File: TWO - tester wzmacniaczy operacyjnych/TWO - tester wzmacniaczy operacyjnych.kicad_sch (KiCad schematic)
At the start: 0 parts

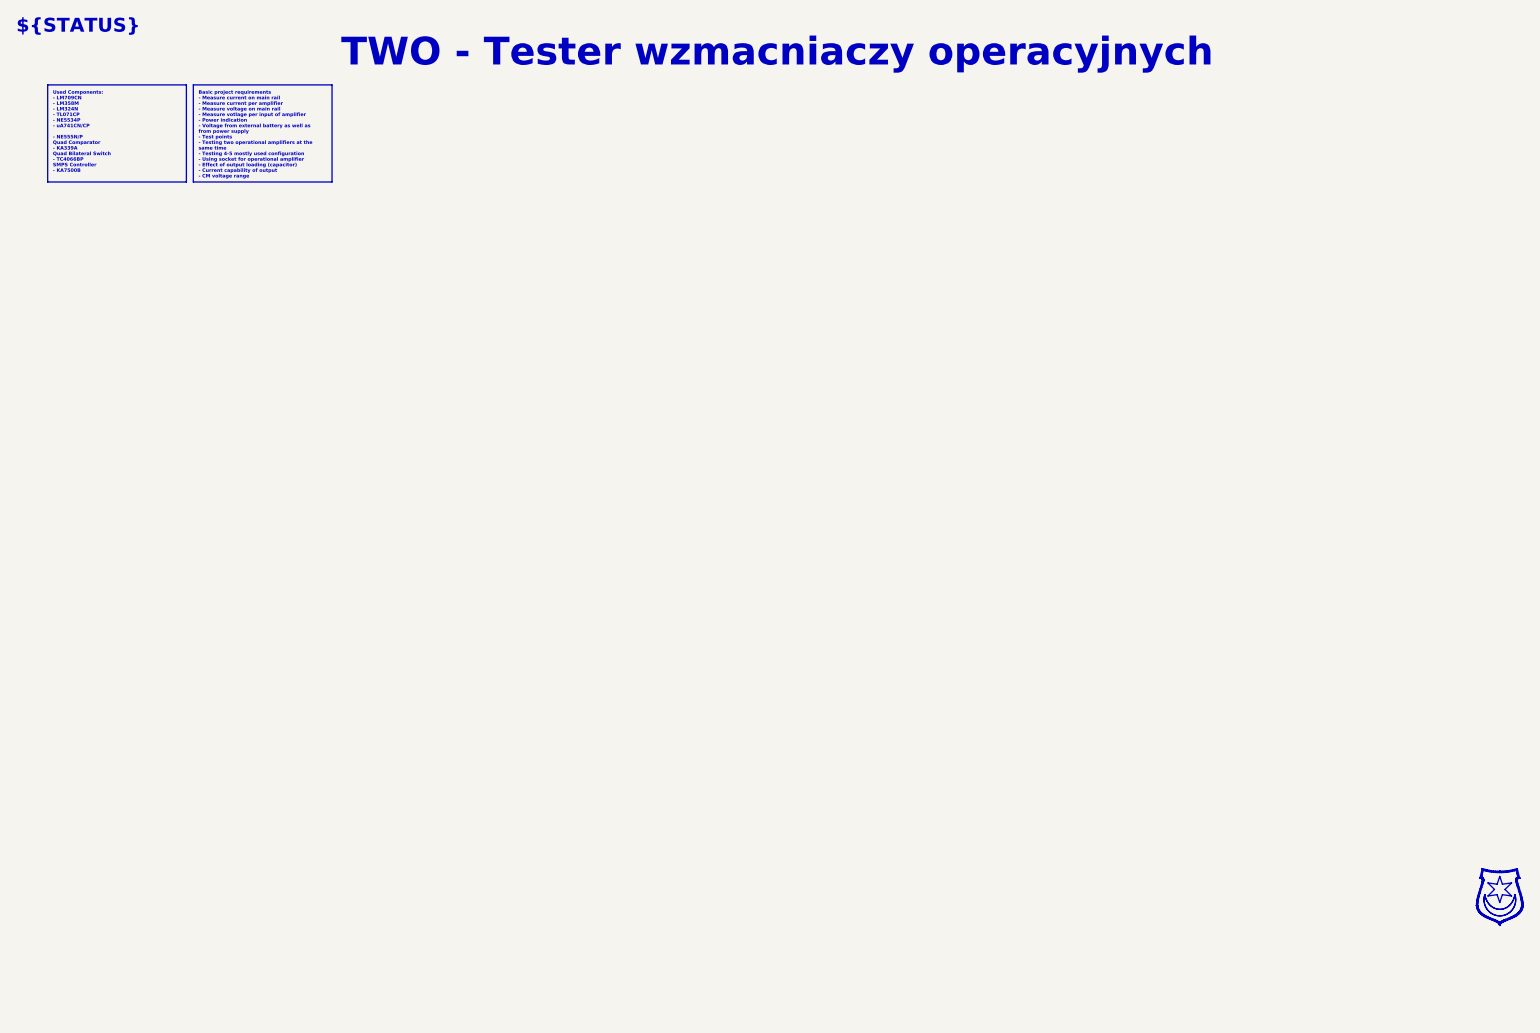
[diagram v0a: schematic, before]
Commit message: Added 0R resistor for 0V potential to measure current, Added on a schematic LM358M, LM324N, TL071CP, NE5534P, uA741CN/CP
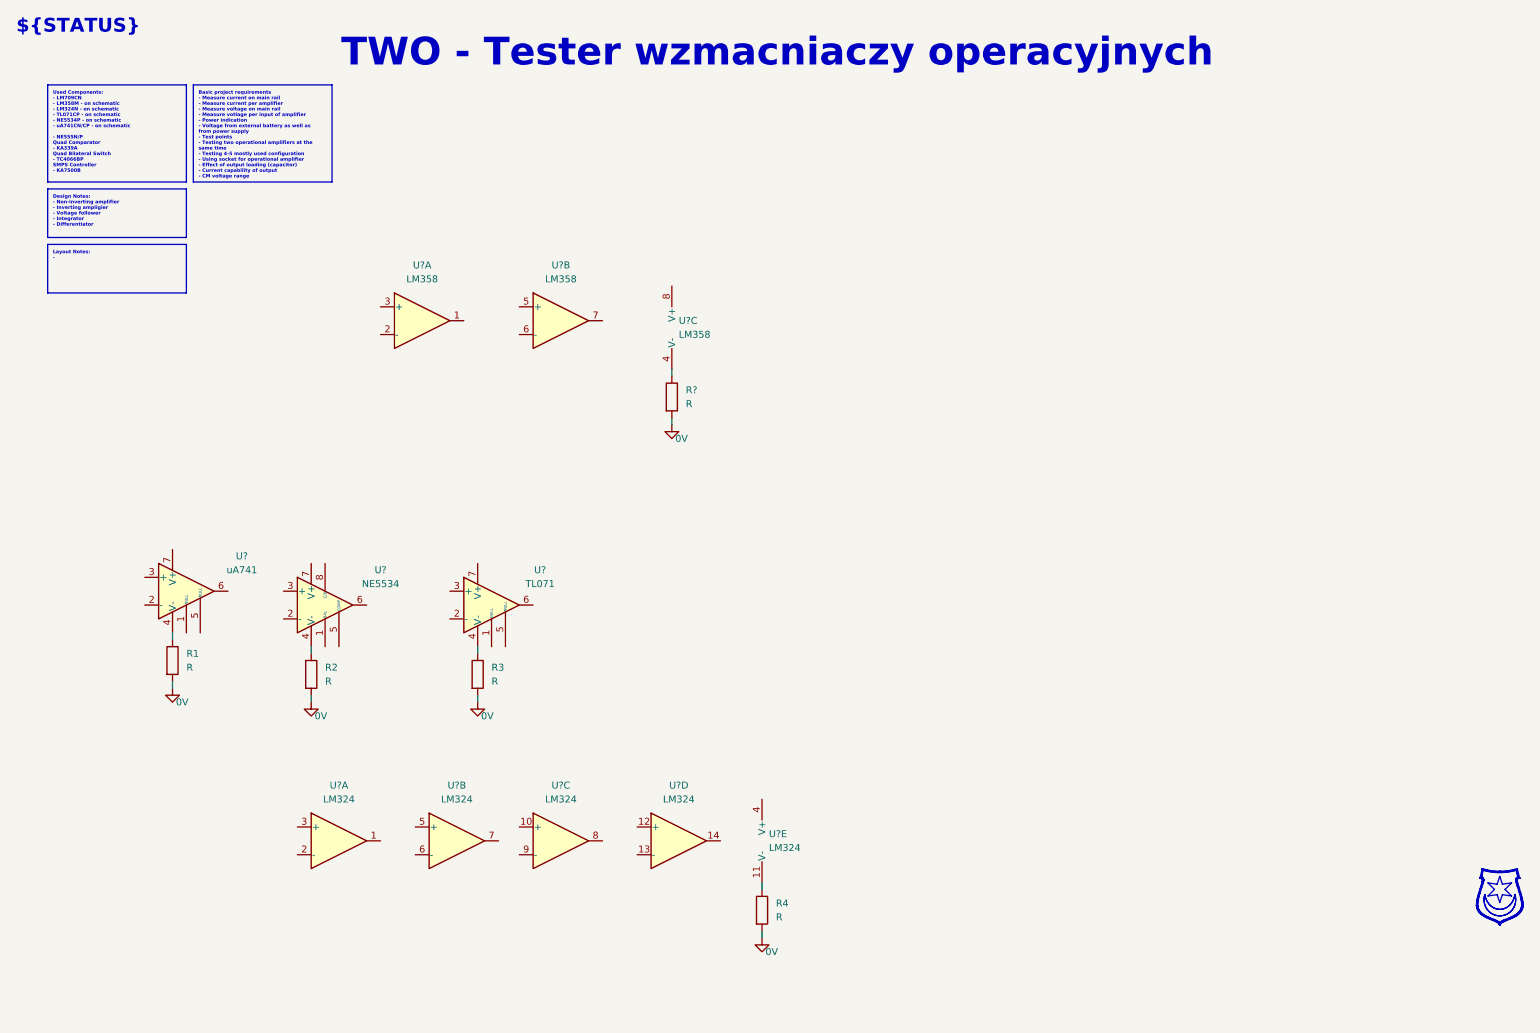
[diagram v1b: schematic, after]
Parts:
- added R1, R2, R3, R4, R?: R, symbol Device:R
- added U? (x5): LM324, symbol Amplifier_Operational:LM324
- added U?: NE5534, symbol Amplifier_Operational:NE5534
- added U?: uA741, symbol Amplifier_Operational:LM741
- added U? (x3): LM358, Package_DIP:DIP-8_W7.62mm_Socket, symbol Amplifier_Operational:LM358
- added U?: TL071, symbol Amplifier_Operational:TL071
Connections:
- new net: R3.1, U?.4 (V-)
- new net: R2.1, U?.4 (V-)
- new net: R4.1, U?.11 (V-)
- new net: R1.1, U?.4 (V-)
- new net: R?.1, U?.4 (V-)
- new net 0V: R1.2, R2.2, R3.2, R4.2, R?.2

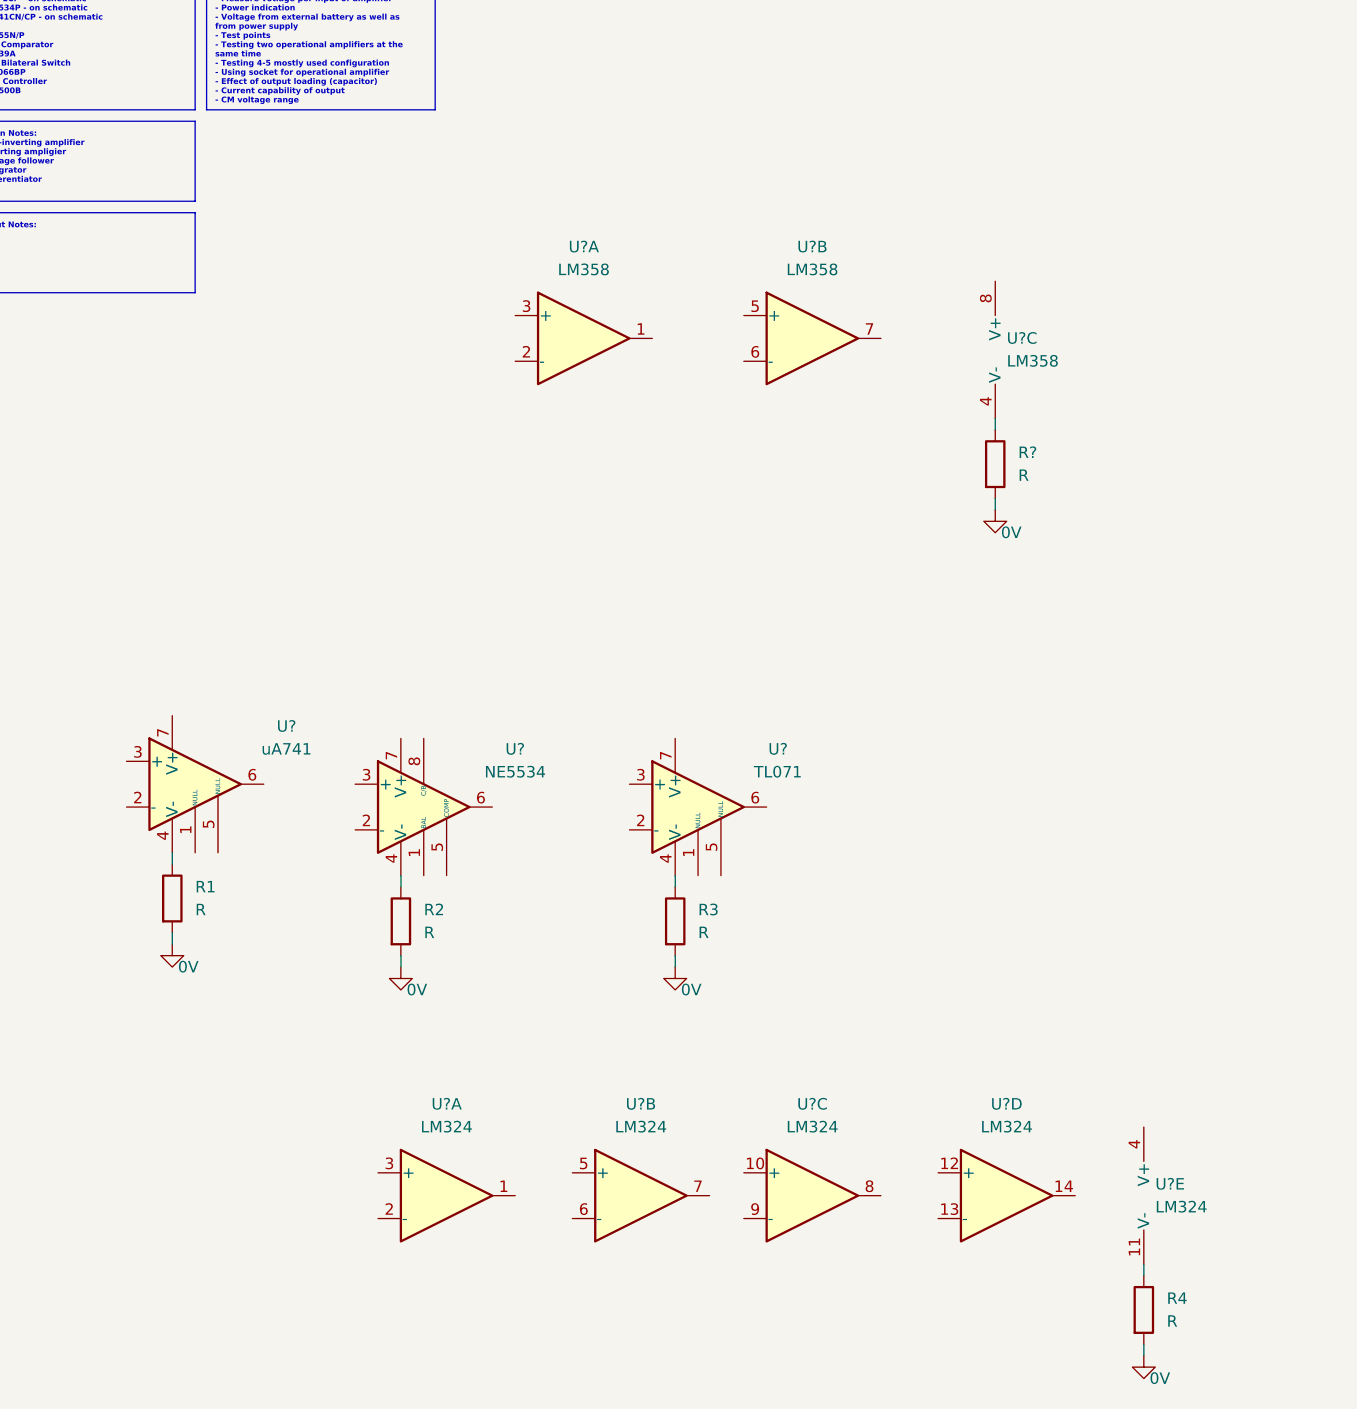
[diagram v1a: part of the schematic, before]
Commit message: Added Positive power supply symbol + 0R resistor to isolate power source
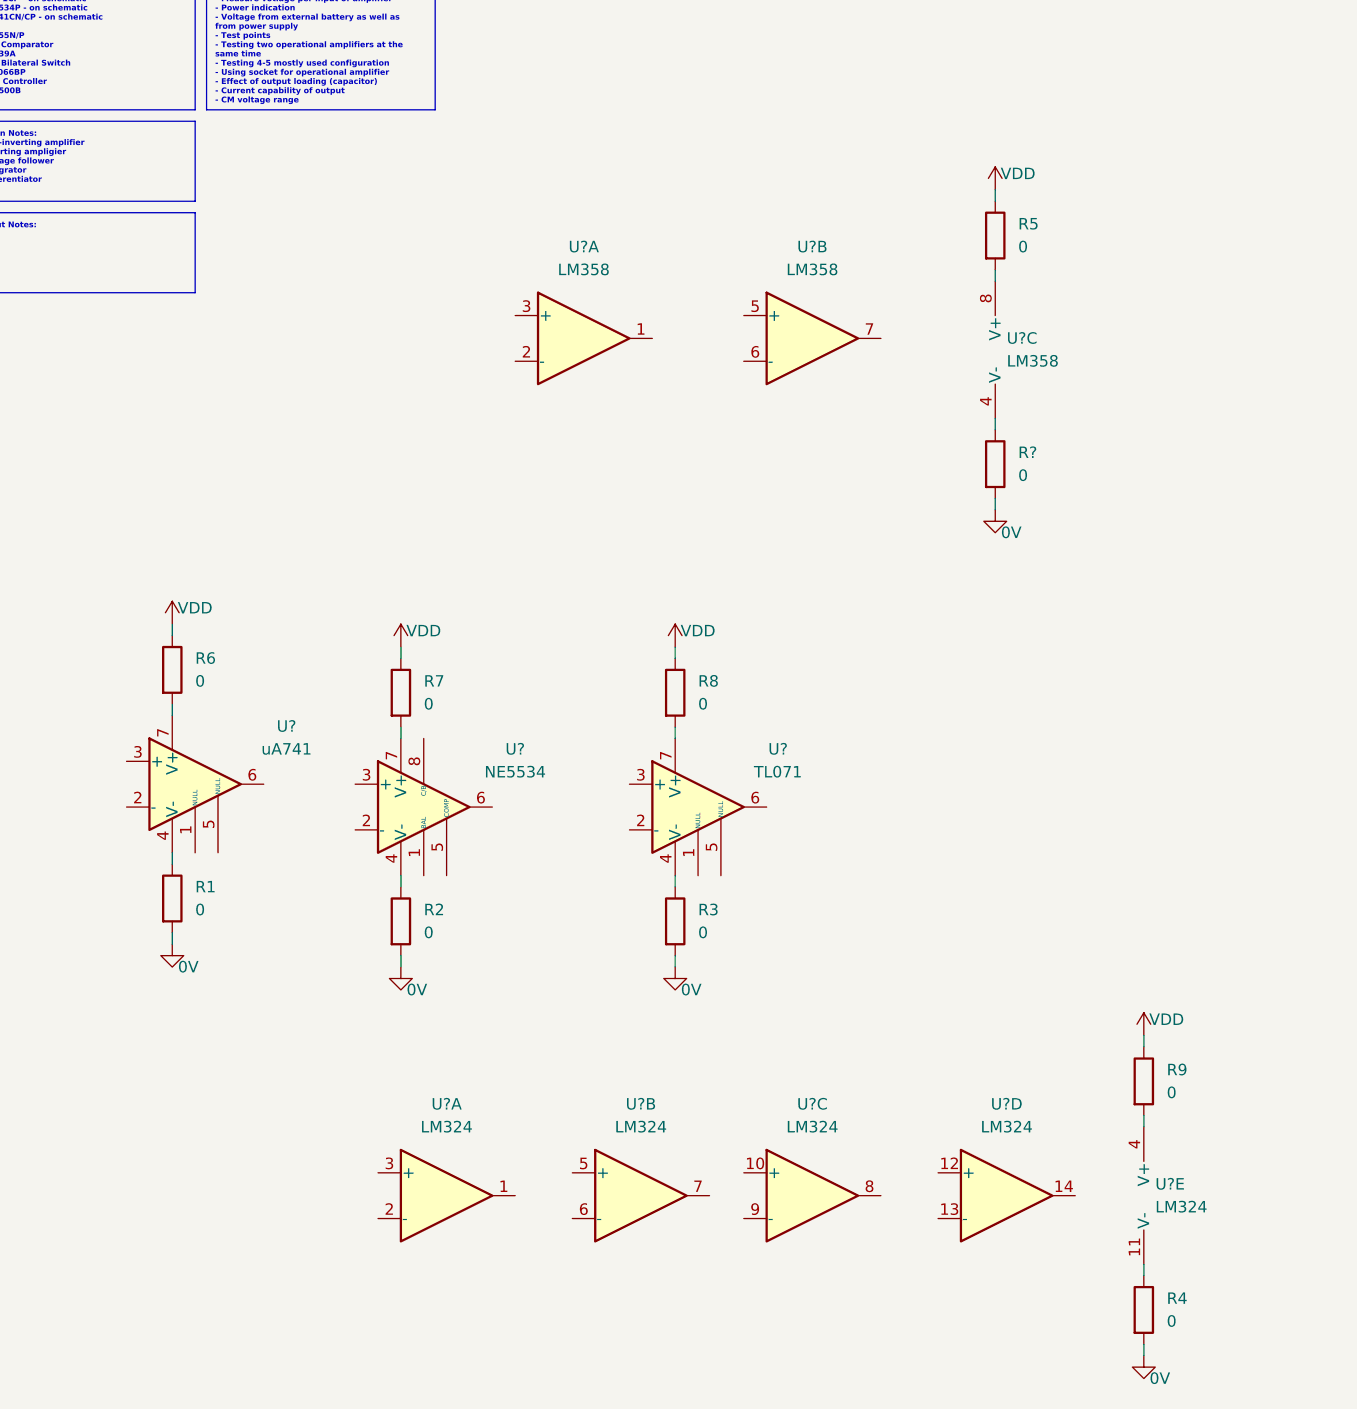
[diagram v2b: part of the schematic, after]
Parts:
- added R5, R6, R7, R8, R9: 0, symbol Device:R
- R1, R2, R3, R4, R?: value R -> 0
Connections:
- net at U?.7 (V+): now also R7.2
- net at U?.4 (V+): now also R9.2
- net at U?.7 (V+): now also R6.2
- net at U?.8 (V+): now also R5.2
- net at U?.7 (V+): now also R8.2
- new net VDD: R5.1, R6.1, R7.1, R8.1, R9.1
